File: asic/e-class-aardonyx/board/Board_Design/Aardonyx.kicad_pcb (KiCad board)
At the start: 4 copper layers, 157.5 x 117.3 mm, 327 parts, among them J1 USB_B_6PIN, J10 Conn_1x6, J11 Conn_1x6, J12 Conn_1x3_M, J13 Conn_1x8_F, J14 Conn_1x6_F, J15 Conn_1x10_F, J16 Conn_1x8_F, J17 USB_OTG, J18 Conn_1x3_M, J19 Conn_1x3_M, J2 Conn_1x8, J3 Conn_1x3_M, J4 Conn_1x4, J5 PJ-202H PWRJACK, J6 Conn_1x3_M, J7 Conn_1x4, J8 Conn_1x3_M, J9 Conn_1x8, Q1 FDN339AN, SW1 SW_SPST, SW2 FSM2JSMAATR, SW3 SW_DIP_x03, U1 FT2232H, U10 TPS7A7002DDAR, U11 ADM1186, U13 TPS7A7002DDAR, U14 74AUP1G09GW, U15 SKT32E, U16 93LC56BT-I_OT, U2 IS42S32160F-TSOP2, U3 CDCE913PW, U4 TPS54627DDAR, U5 CAT24M01WI-GT3, U6 IS25LP256x-xM, U7 ADC128S102CIMTX/NOPB, U8 LSF0108PWR, U9 LSF0108PWR, Y1 12MHz, Y2 27MHz

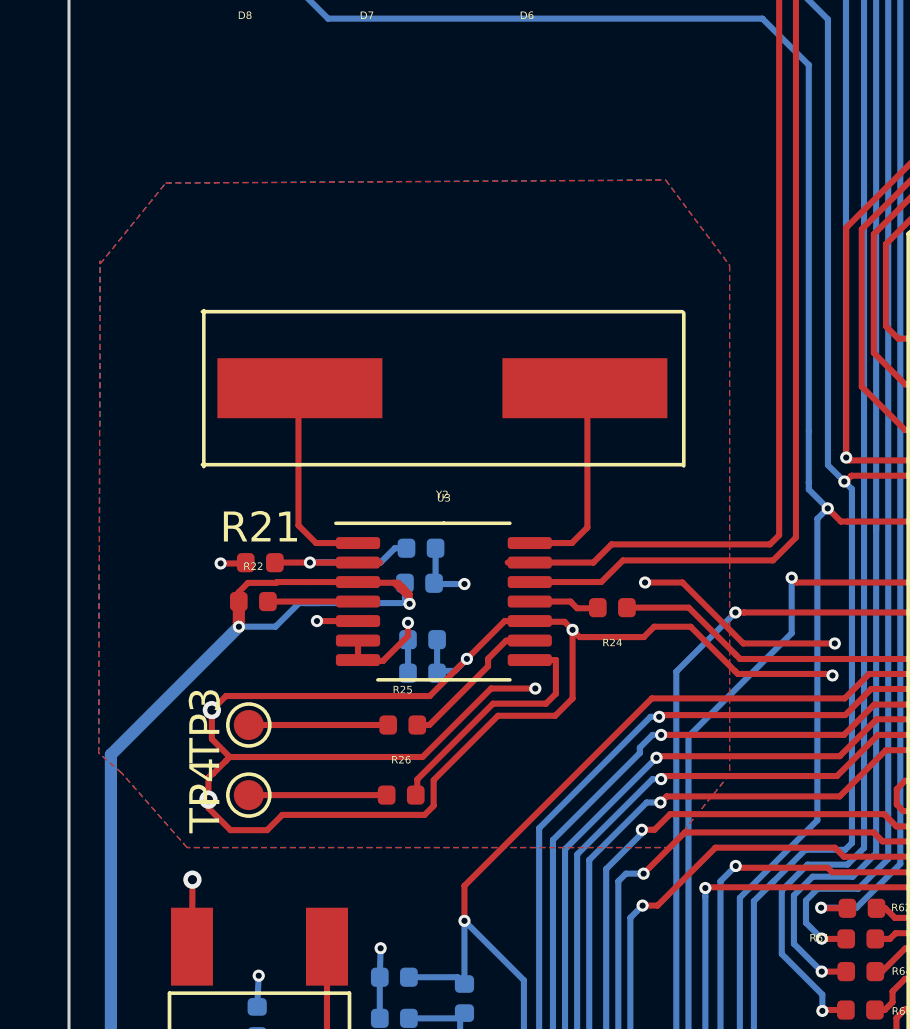
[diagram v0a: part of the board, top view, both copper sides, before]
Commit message: Adding capacitors to clock
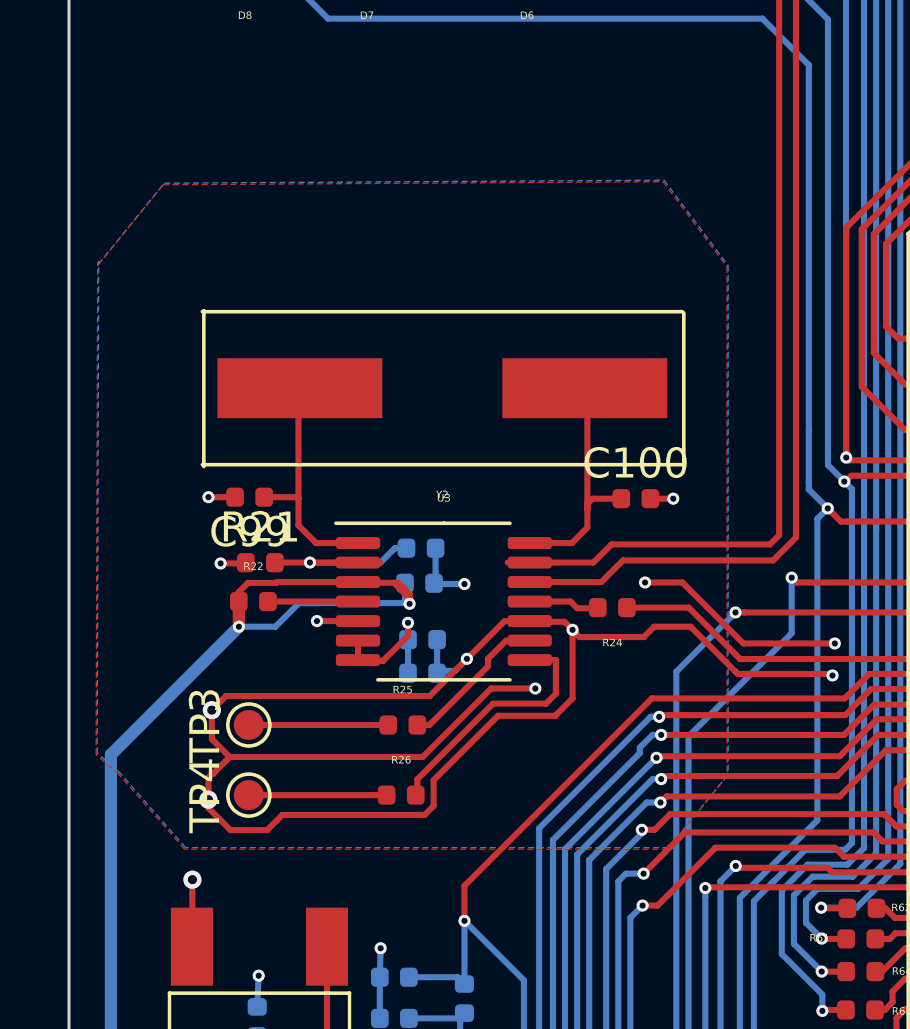
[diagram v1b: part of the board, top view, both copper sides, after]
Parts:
- added C100: 18PF,0402, Capacitor_SMD:C_0402_1005Metric, F.Cu at (142.1, 76.3)
- added C99: 18PF,0402, Capacitor_SMD:C_0402_1005Metric, F.Cu at (129.2, 76.3)
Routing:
- net GND: track 357.9 -> 359.6 mm, vias 175 -> 177
- net Net-(C100-Pad1): track 6.85 -> 8.22 mm
- net Net-(C99-Pad1): track 6.90 -> 8.06 mm

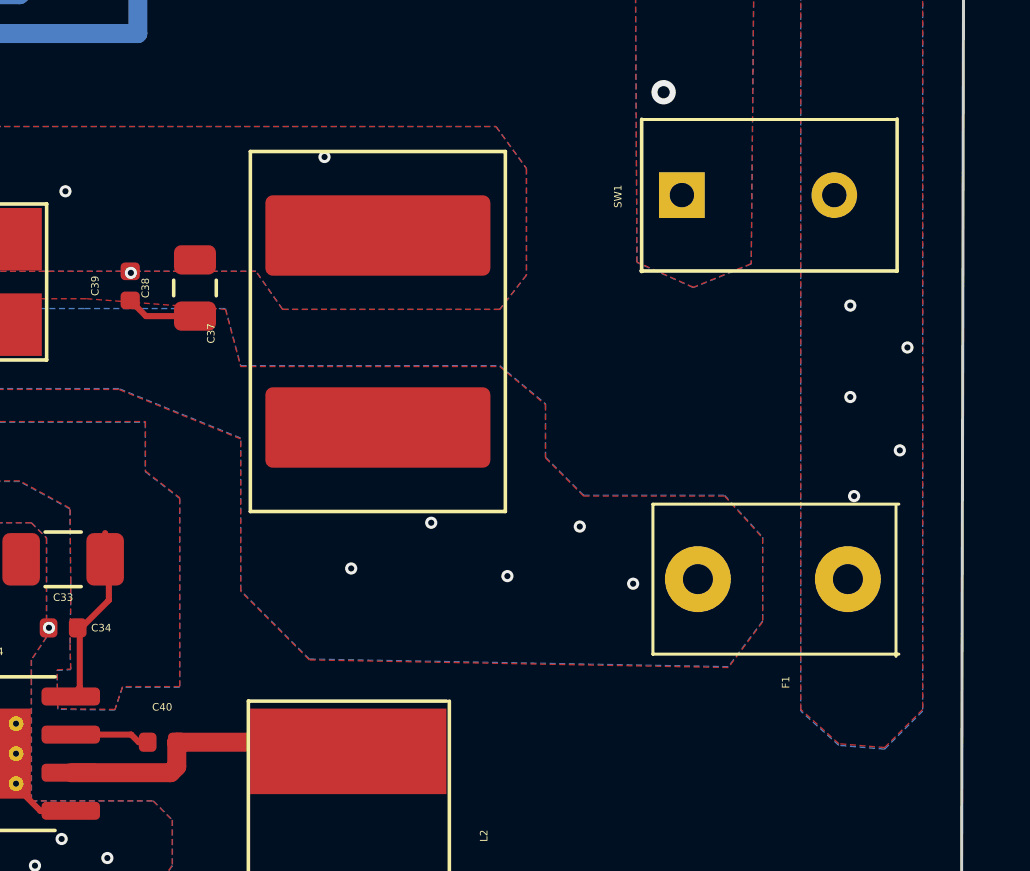
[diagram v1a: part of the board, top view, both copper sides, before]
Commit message: updated footprint c37 & f1
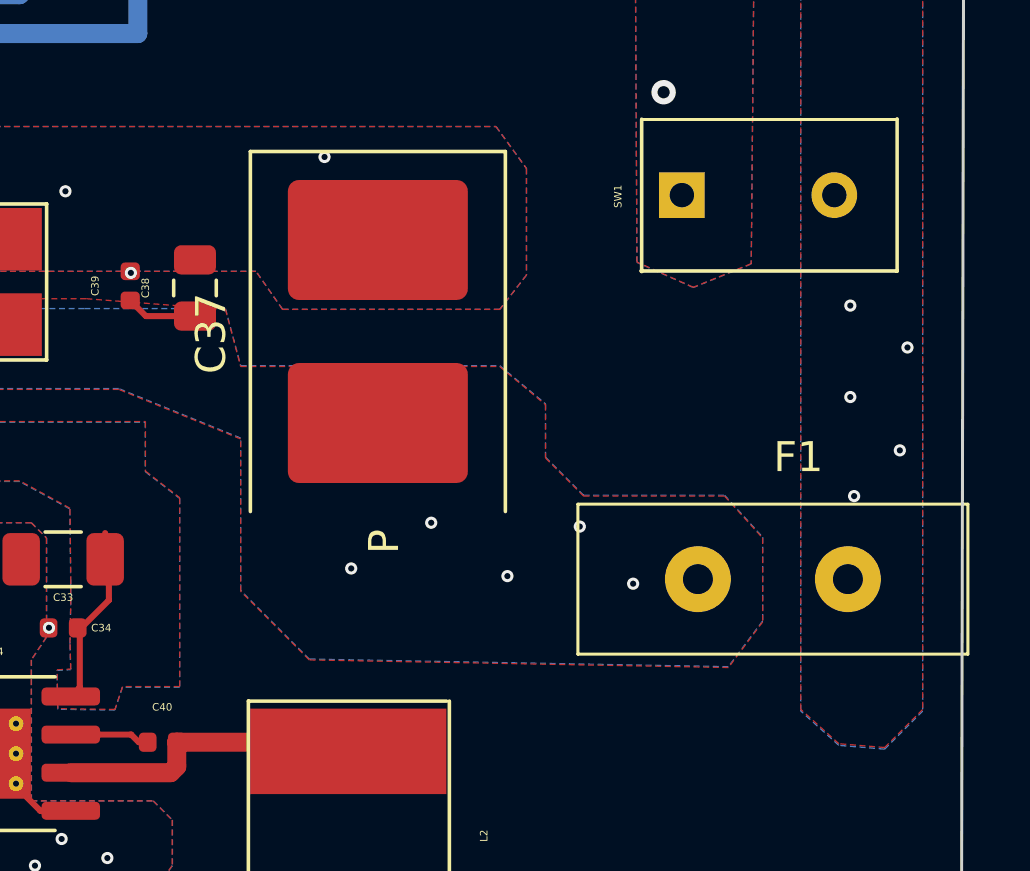
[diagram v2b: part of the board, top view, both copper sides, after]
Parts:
- C37: footprint Aardonyx:CP_EIA-7260-38_VISHAY_Pad2.68x7.50mm_HandSolder -> Aardonyx:CP_EIA-2924_tcn4227_Pad6.1x7.3mm
- F1: footprint Aardonyx:vishay_ptccl_d1mm_w5mm -> Aardonyx:vishay_ptccl_d12.5mm_w4mm

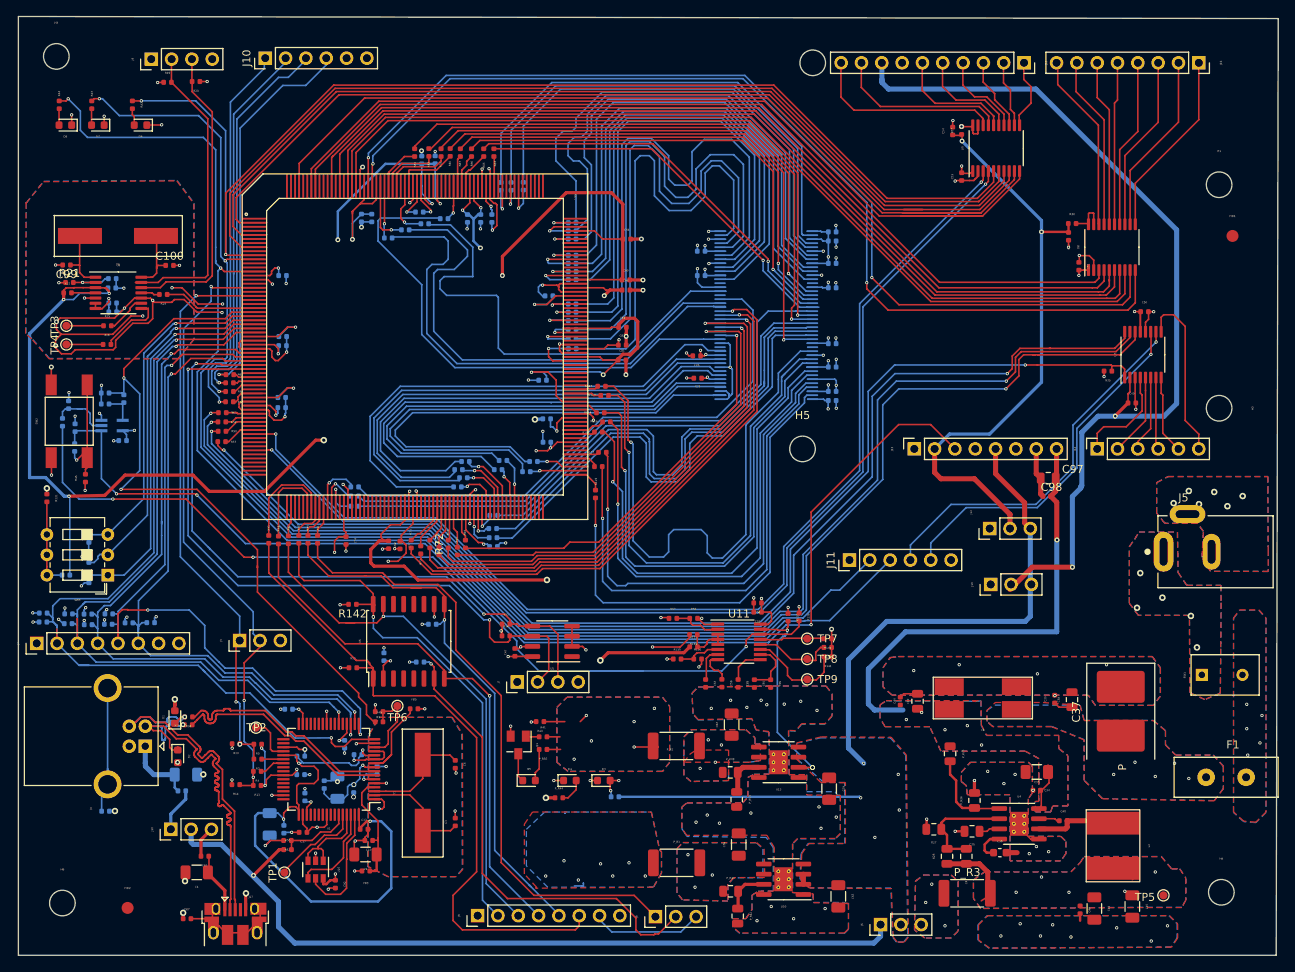
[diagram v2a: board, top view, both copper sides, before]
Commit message: Updating layout after back annotation
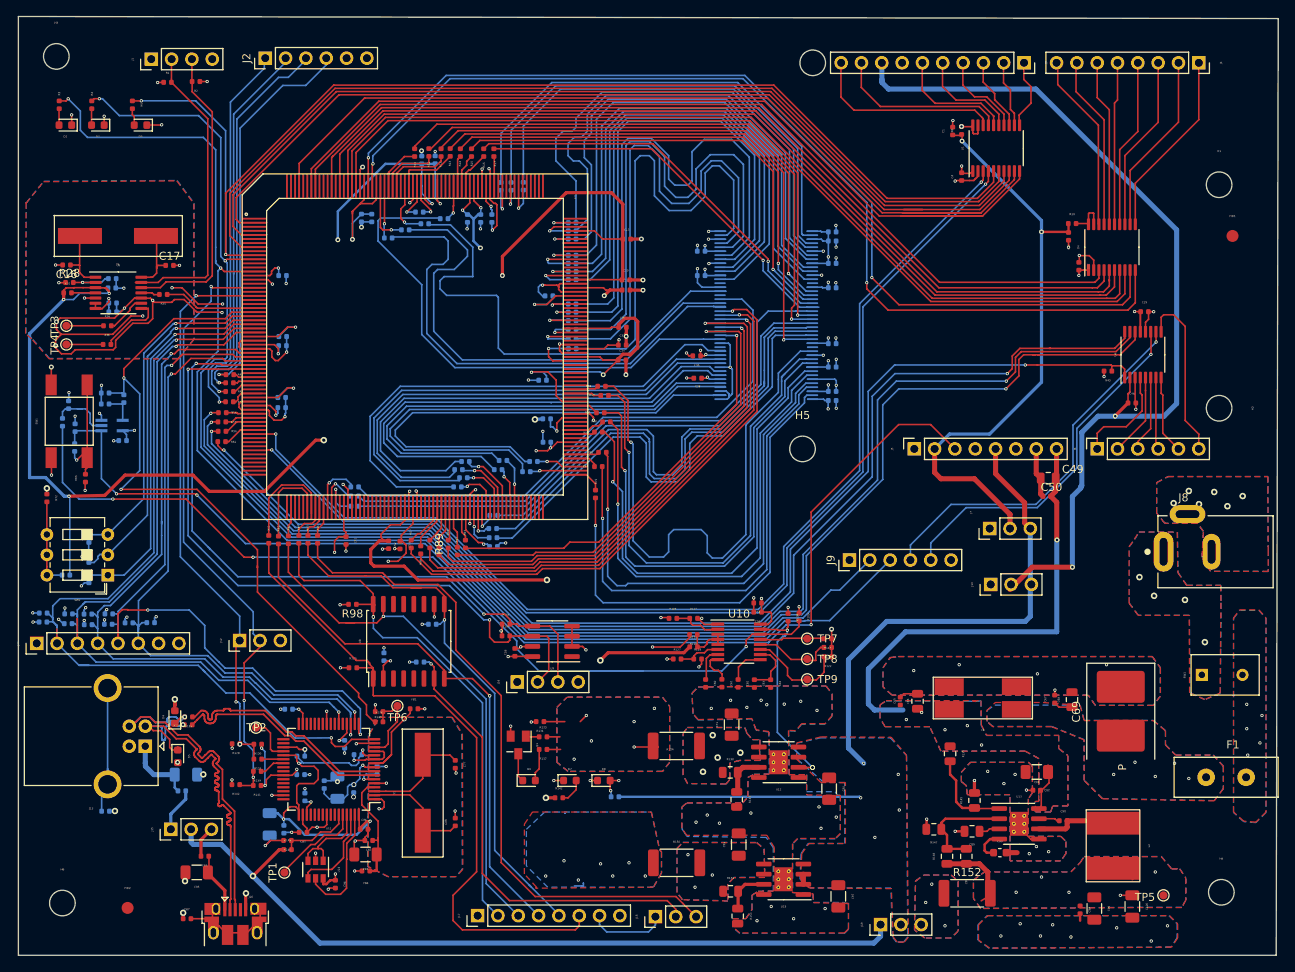
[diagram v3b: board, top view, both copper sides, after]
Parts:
- renumbered C54 to C1, C88 to C10, C45 to C100, C52 to C11, C18 to C12, C64 to C13, C19 to C14, C28 to C15, C99 to C16, C100 to C17, C20 to C18, C65 to C19, C82 to C2, C89 to C20, C27 to C21, C51 to C22, C30 to C23, C87 to C24, C86 to C25, C21 to C26, C31 to C27, C32 to C28, C50 to C29, C79 to C3, C84 to C30, C63 to C31, C68 to C32, C83 to C33, C81 to C34, C22 to C35, C26 to C36, C78 to C37, C25 to C38, C80 to C39, C53 to C4, C29 to C40, C66 to C41, C71 to C42, C23 to C43, C60 to C44, C24 to C45, C49 to C46, C61 to C47, C75 to C48, C97 to C49, C76 to C5, C98 to C50, C74 to C51, C69 to C52, C77 to C53, C72 to C54, C94 to C55, C93 to C56, C48 to C57, C47 to C58, C15 to C59, C73 to C6, C57 to C60, C58 to C61, C85 to C62, C95 to C63, C96 to C64, C44 to C65, C42 to C66, C39 to C67, C38 to C68, C37 to C69, C90 to C7, C14 to C70, C62 to C71, C12 to C72, C11 to C73, C91 to C74, C7 to C75, C16 to C76, C6 to C77, C8 to C78, C5 to C79, C70 to C8, C59 to C80, C33 to C81, C34 to C82, C2 to C83, C4 to C84, C17 to C85, C13 to C86, C10 to C87, C3 to C88, C35 to C89, C67 to C9, C40 to C90, C56 to C91, C41 to C92, C36 to C93, C9 to C94, C1 to C95, C92 to C96, C55 to C97, C46 to C98, C43 to C99, D8 to D1, D7 to D2, D6 to D3, D1 to D4, D2 to D5, D5 to D6, D4 to D7, D3 to D8, FB5 to FB1, FB6 to FB3, FB3 to FB4, FB1 to FB5, FB4 to FB6, J4 to J1, J19 to J10, J2 to J11, J3 to J12, J1 to J13, J7 to J14, J18 to J15, J17 to J16, J9 to J17, J8 to J18, J6 to J19, J10 to J2, J15 to J3, J16 to J4, J13 to J5, J14 to J6, J12 to J7, J5 to J8, J11 to J9, R19 to R1, R82 to R10, R7 to R100, R11 to R101, R16 to R102, R31 to R103, R33 to R104, R34 to R105, R53 to R106, R56 to R107, R137 to R108, R138 to R109, R83 to R11, R6 to R110, R8 to R111, R12 to R112, R15 to R113, R18 to R114, R17 to R115, R134 to R116, R139 to R117, R133 to R118, R140 to R119, R78 to R12, R30 to R120, R32 to R121, R141 to R122, R38 to R123, R39 to R124, R1 to R125, R49 to R126, R135 to R127, R136 to R128, R10 to R129, R80 to R13, R9 to R130, R40 to R131, R3 to R132, R41 to R133, P_R2 to R134, P_R25 to R135, R2 to R136, P_R56 to R137, P_R49 to R138, R4 to R139, R87 to R14, R14 to R140, R13 to R141, P_R44 to R142, R29 to R143, P_R50 to R144, P_R26 to R145, R52 to R146, R27 to R147, R28 to R148, R50 to R149, R86 to R15, P_R1 to R150, P_R41 to R151, P_R3 to R152, P_R42 to R153, R85 to R16, R84 to R17, R36 to R18, R81 to R19, R20 to R2, R99 to R20, R79 to R21, R100 to R22, R88 to R23, R89 to R24, R101 to R25, R102 to R26, R103 to R27, R21 to R28, R23 to R29, R44 to R3, R104 to R30, R105 to R31, R22 to R32, R106 to R33, R107 to R34, R24 to R35, R25 to R36, R108 to R37, R109 to R38, R26 to R39, R43 to R4, R110 to R40, R111 to R41, R62 to R42, R35 to R43, R61 to R44, R55 to R45, R54 to R46, R64 to R47, R112 to R48, R113 to R49, R42 to R5, R48 to R50, R63 to R52, R47 to R53, R60 to R54, R59 to R55, R58 to R56, R114 to R57, R116 to R58, R115 to R59, R37 to R6, R46 to R60, R57 to R61, R117 to R62, R45 to R63, R124 to R64, R122 to R65, R120 to R66, R118 to R67, R125 to R68, R123 to R69, R96 to R7, R121 to R70, R126 to R71, R131 to R72, R77 to R73, R127 to R74, R119 to R75, R75 to R77, R65 to R78, R66 to R79, R97 to R8, R128 to R80, R95 to R81, R93 to R82, R92 to R83, R90 to R84, R94 to R85, R91 to R86, R74 to R87, R73 to R88, R72 to R89, R98 to R9, R71 to R90, R70 to R91, R69 to R92, R68 to R93, R67 to R94, R129 to R95, R132 to R96, R130 to R97, R142 to R98, R5 to R99, SW2 to SW1, SW3 to SW2, SW1 to SW3, U9 to U1, U11 to U10, U1 to U11, U13 to U12, U4 to U13, U16 to U14, U10 to U15, U15 to U2, U2 to U3, U8 to U4, U3 to U5, U7 to U6, U14 to U7, U6 to U8, U5 to U9, Y2 to Y1, Y1 to Y2
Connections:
- J18 pad 1: /arduino_header/QSPI0_NCS -> /arduino_header/QSPI0_NCS_H
- J18 pad 3: /arduino_header/QSPI0_NCS_H -> /arduino_header/QSPI0_NCS
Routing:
- net VCORE_FTDI: track 74.7 -> 50.9 mm
- net /arduino_header/QSPI0_NCS: track 78.4 -> 83.4 mm
- net /arduino_header/QSPI0_NCS_H: track 14.0 -> 9.90 mm
- net /arduino_header/QSPI0_NCS_F: track 59.0 -> 56.8 mm
- net VBUS: track 102.1 -> 100.2 mm
- net GND: track 359.6 -> 361.2 mm
- net VCC5V: track 11.1 -> 12.6 mm
- net Net-(J8-Pad1): vias 5 -> 4

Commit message: Updating symbols for USB
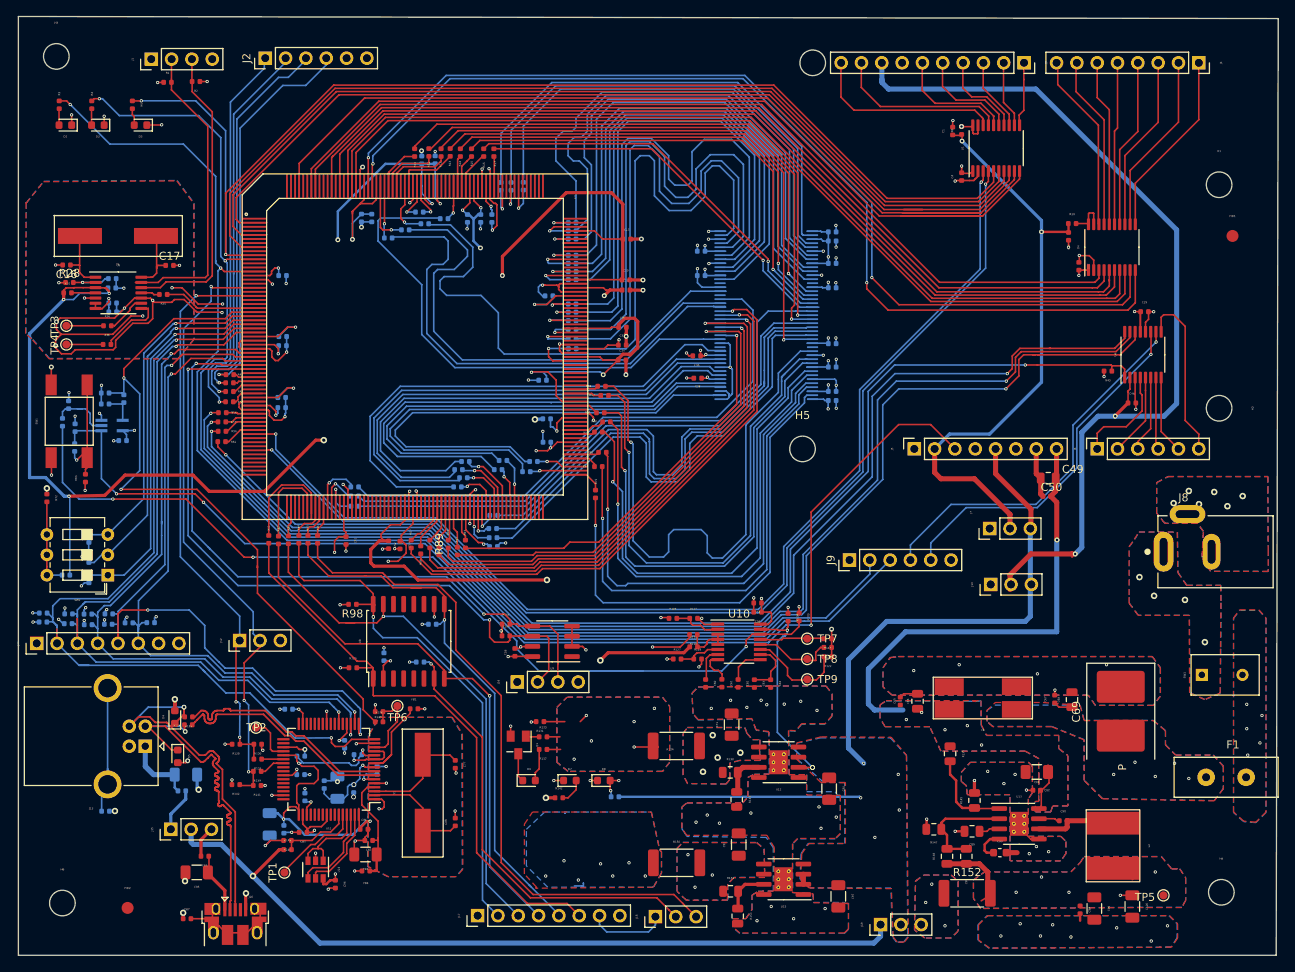
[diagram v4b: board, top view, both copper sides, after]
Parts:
- moved R129 0.06 mm to (150.4, 136.2)
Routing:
- net /arduino_header/QSPI0_IO3: track 86.8 -> 74.9 mm
- net V3P3: track 195.7 -> 188.7 mm
- net /ftdi/USB_D-: track 51.1 -> 46.1 mm
- net Net-(U11-Pad63): track 15.1 -> 10.9 mm
- net /arduino_header/IO_15: track 168.9 -> 165.3 mm
- net GND: track 361.2 -> 364.0 mm
- net /arduino_header/QSPI0_NCS_F: track 56.8 -> 54.5 mm
- net /sdram/SDRAM_DQM1: track 61.8 -> 60.0 mm
- net Net-(C74-Pad1): track 9.66 -> 11.1 mm
- net /arduino_header/IO_14: track 162.0 -> 163.2 mm
- net VAC: track 116.3 -> 117.2 mm
- net /arduino_header/AH_IO_8: track 8.81 -> 8.07 mm
